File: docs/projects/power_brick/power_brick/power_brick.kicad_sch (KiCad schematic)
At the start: 17 parts, among them J1 Conn_01x02, J2 Conn_01x02, J3 Conn_01x02, U1 TPS54302, U10 C_22uF_0805, U11 C_100nF_0402, U12 L_10uH_1210, U13 R_31.6k_0603, U14 R_10k_0603, U2 C_10uF_0805, U3 C_22uF_0805, U4 C_100nF_0402, U5 L_10uH_1210, U6 R_52.3k_0603, U7 R_10k_0603, U8 TPS54302, U9 C_10uF_0805

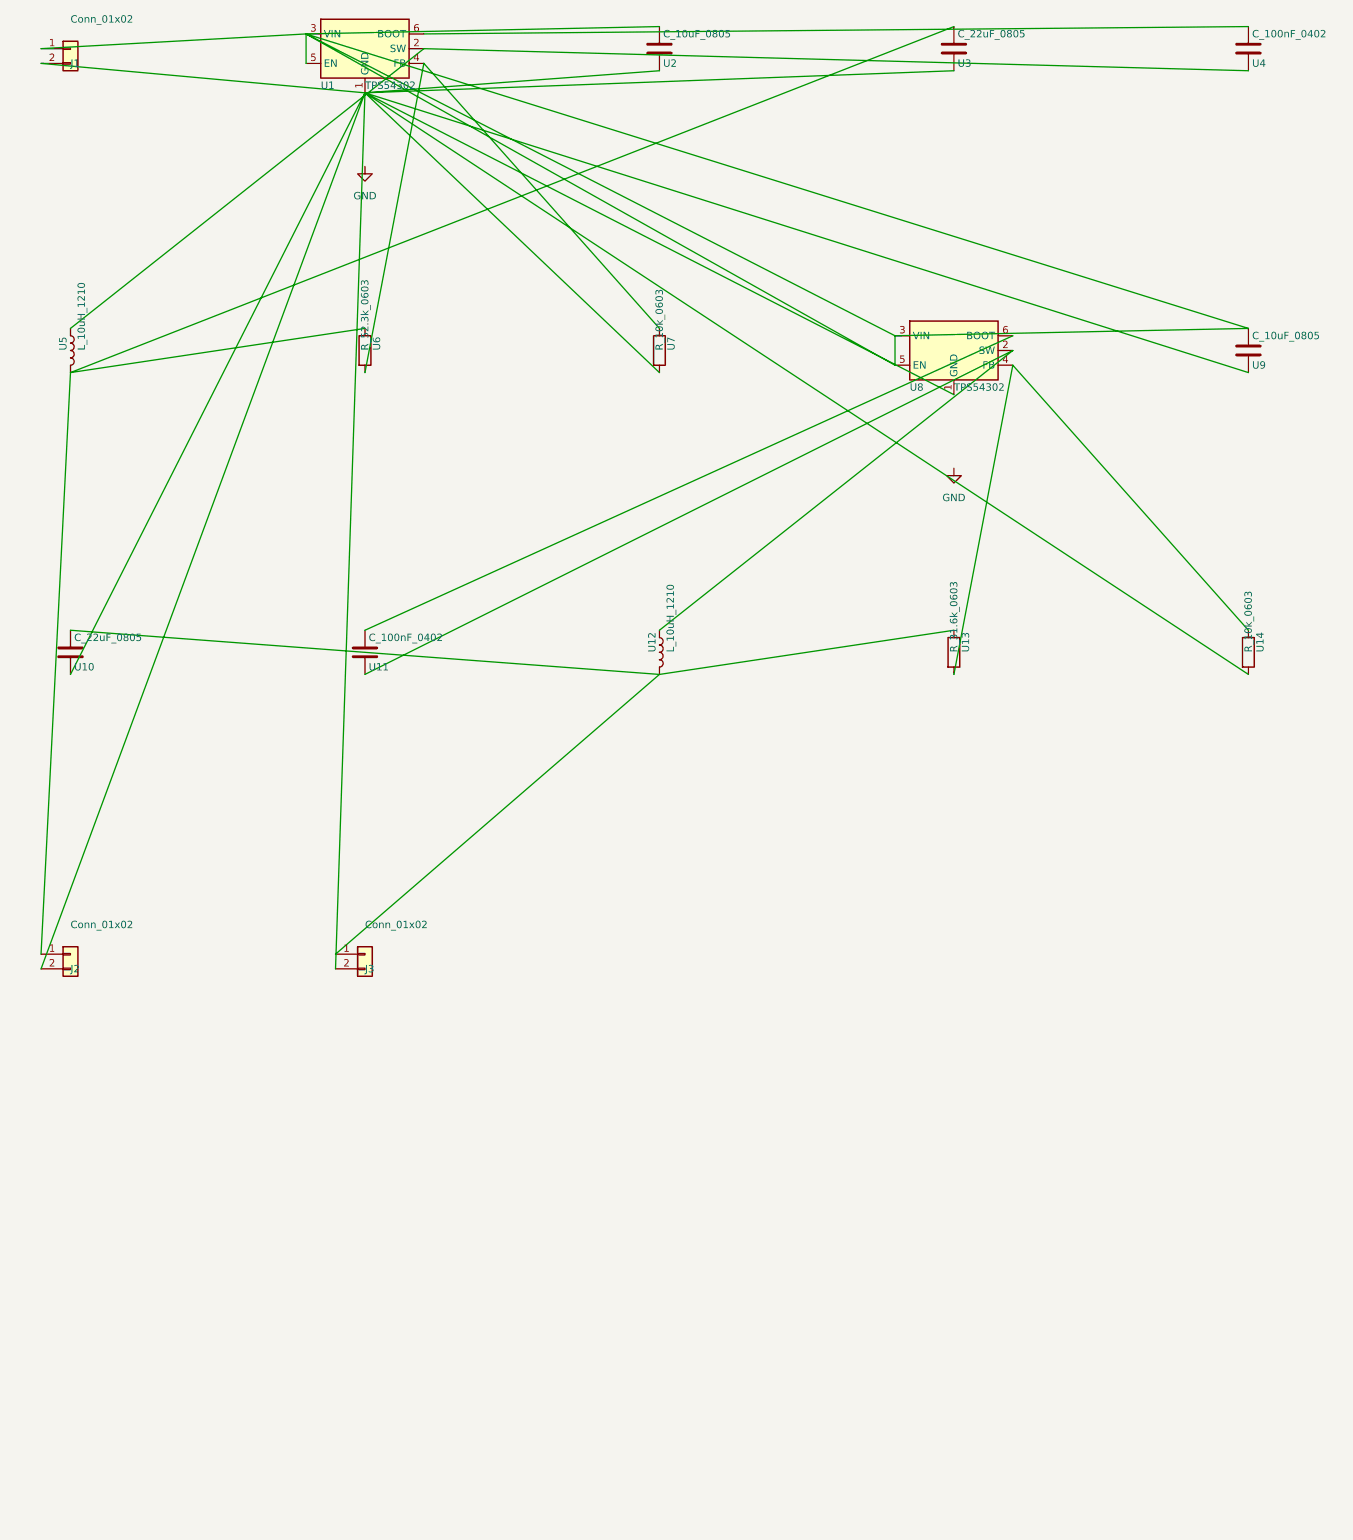
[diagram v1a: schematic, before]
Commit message: Auto-layout A1: cluster factory blocks (Buck + its passives)
Placement now groups parts that share a `group` into one tight mini-grid
block, then packs blocks left-to-right (wrapping past _PAGE_W_MM). The
Buck factory tags its IC + Cin/Cout/L/Cboot + feedback divider with
group=id, so each regulator lays out as a coherent cluster instead of its
passives scattering across the sheet — internal wires stay short and the
two bucks in power_brick read as two distinct blocks.

- SubsystemPick.group (placement cluster hint).
- _place_subsystems(): group → mini-grid per cluster, block packing with
  page-width wrap. Replaces the flat per-part grid.

This is auto-layout stage A1 (clustering). Net-aware ordering WITHIN a
cluster (A2) and an orthogonal wire router (A3) are the remaining levers
for crossing-free wiring — judge correctness from ERC, not aesthetics.

Regenerate the 3 example schematics + rendered SVGs.

Co-Authored-By: Claude Opus 4.8 (1M context) <noreply@anthropic.com>
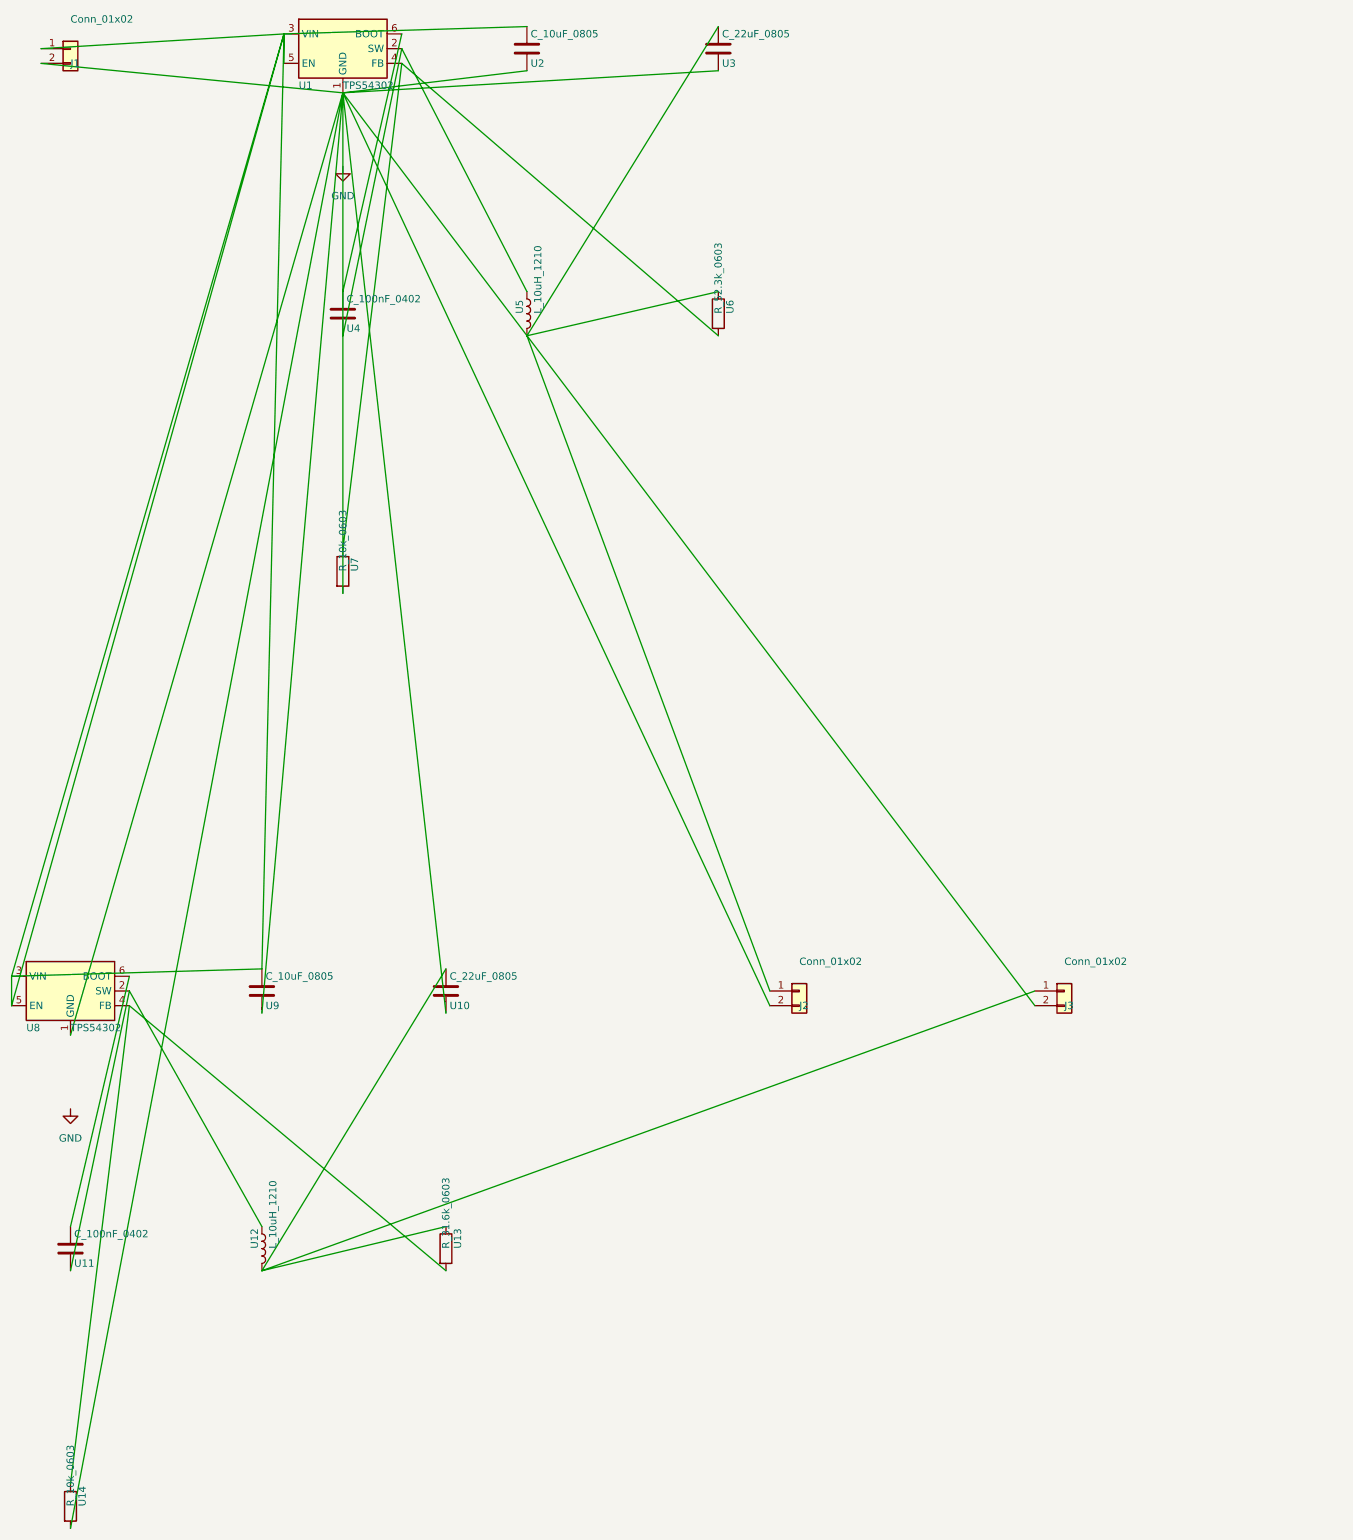
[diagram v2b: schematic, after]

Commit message: Regenerate examples + ELK layout tests
Re-execute power_brick / can_servo / sensor_node through the mandatory
ELK path; schematics now route with clean orthogonal wires that meet
pins, ERC clean (0 real / 0 expected on ERC_REAL_SYMBOL_CODES). Refresh
the tracked rendered SVGs.

Add tests/test_elk_layout.py: ELK raises LayoutError when node/the bridge
is unavailable (no fallback), and every routed wire is axis-aligned,
grid-snapped, and lands its pins on the routed endpoints.

Co-Authored-By: Claude Opus 4.8 (1M context) <noreply@anthropic.com>
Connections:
- net GND: now also J1.2 (Pin_2), J2.2 (Pin_2), J3.2 (Pin_2), U1.1 (GND), U10.2, U14.2, U2.2, U3.2, U7.2, U8.1 (GND), U9.2
